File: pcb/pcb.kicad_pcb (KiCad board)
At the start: 2 copper layers, 58.9 x 71 mm, 19 parts, among them J1 CW308_WEST, J3 CW308_EAST, J4 CW308_SOUTH, J5 DEBUG, P1 WEST_PINS, P3 EAST_PINS, P4 SOUTH_PINS, SW1 RESET, U1 MSPM0L2228SPMR

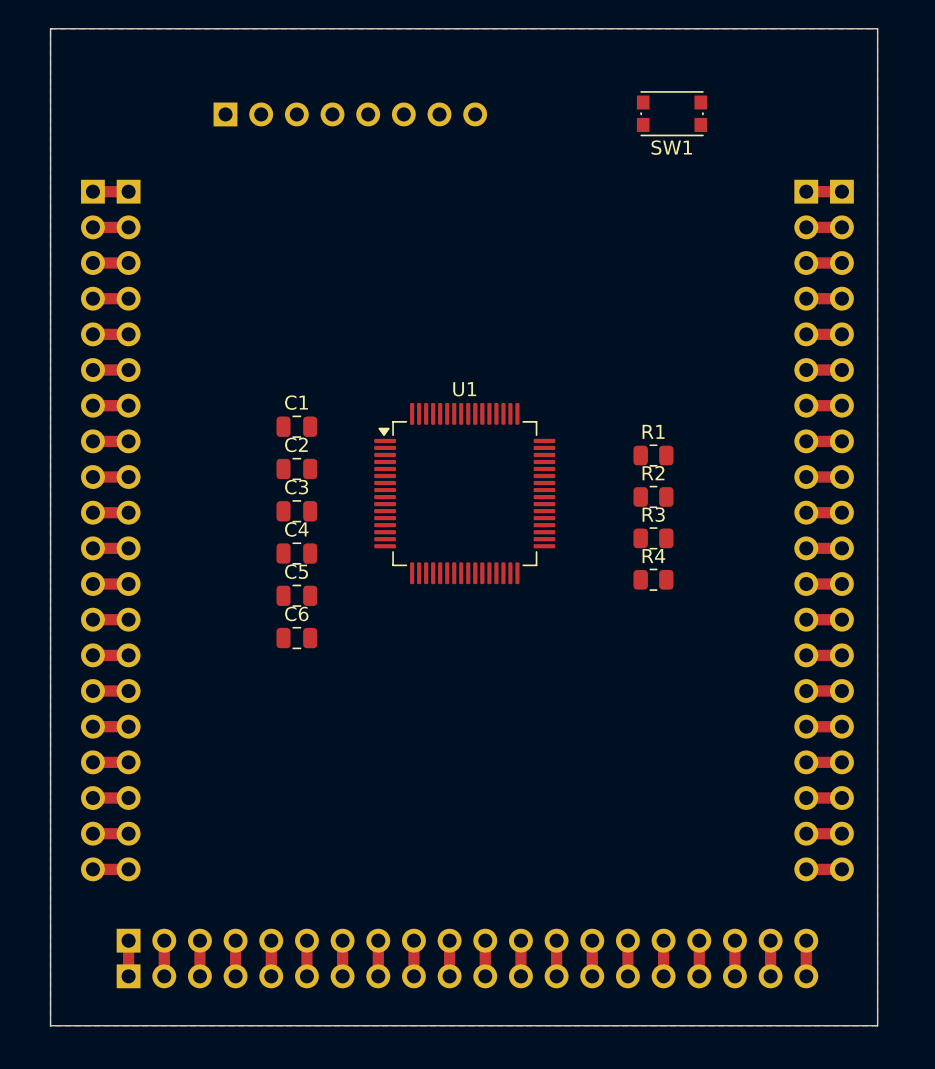
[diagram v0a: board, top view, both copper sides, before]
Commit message: PCB: auto-place and single-sided route, wire-jumper holes
Moved U1, the passives and SW1 (headers stay locked) and routed every
net on F.Cu only, with no vias. The 8 connections a single layer cannot
make get through-hole landing pads W1A..W8B (W2 lands on the J1-10 pin)
for wire jumpers on the back side.

Co-Authored-By: Claude Opus 5.5 <noreply@anthropic.com>
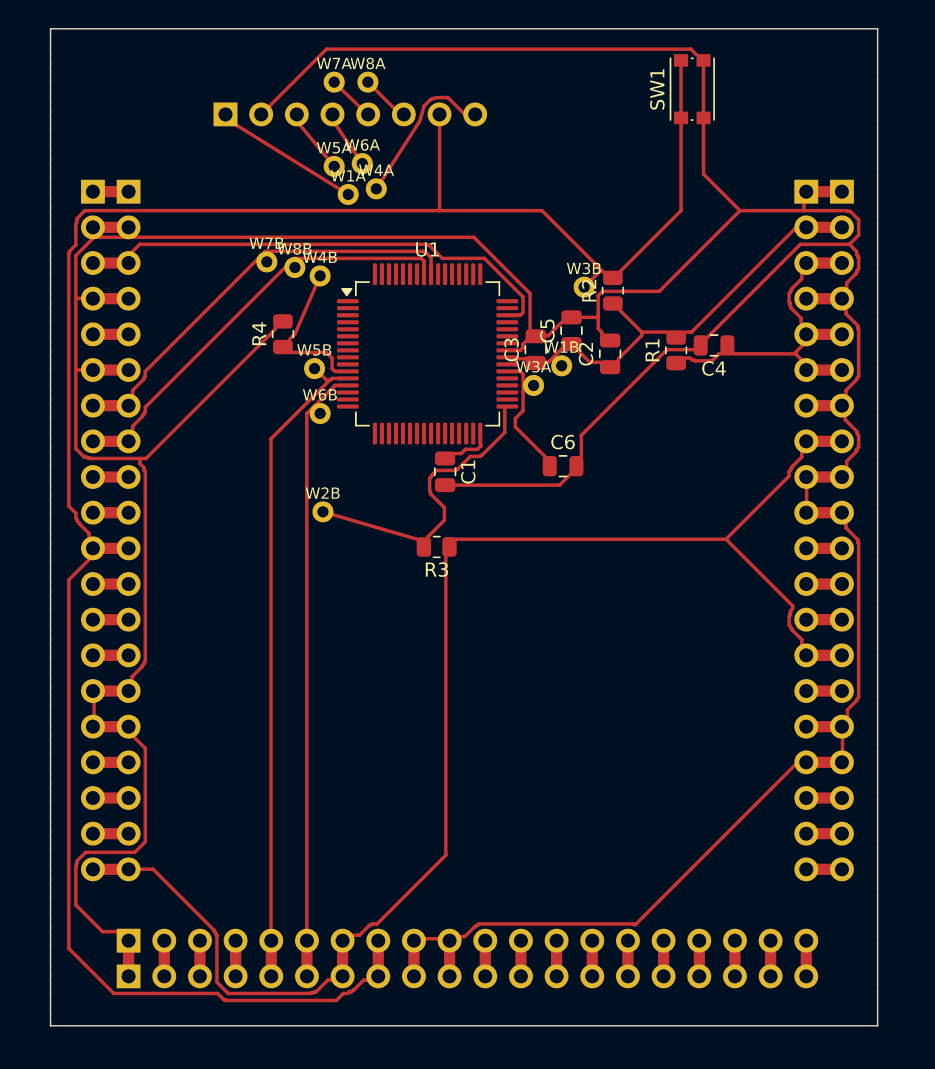
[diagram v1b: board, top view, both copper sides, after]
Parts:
- added W1A: Wire, , F.Cu at (69.7, 89.2)
- added W1B: Wire, , F.Cu at (84.9, 101.4)
- added W2B: Wire, , F.Cu at (67.9, 111.8)
- added W3A: Wire, , F.Cu at (82.9, 102.8)
- added W3B: Wire, , F.Cu at (86.5, 95.8)
- added W4A: Wire, , F.Cu at (71.7, 88.8)
- added W4B: Wire, , F.Cu at (67.7, 95.0)
- added W5A: Wire, , F.Cu at (68.7, 87.2)
- added W5B: Wire, , F.Cu at (67.3, 101.6)
- added W6A: Wire, , F.Cu at (70.7, 87.0)
- added W6B: Wire, , F.Cu at (67.7, 104.8)
- added W7A: Wire, , F.Cu at (68.7, 81.2)
- added W7B: Wire, , F.Cu at (63.9, 94.0)
- added W8A: Wire, , F.Cu at (71.1, 81.2)
- added W8B: Wire, , F.Cu at (65.9, 94.4)
- moved C4 33.2 mm to (95.8, 100.0), turned to 180 degrees
- moved R4 31.7 mm to (65.0, 99.2), turned to 90 degrees
- moved C5 27.2 mm to (85.6, 98.9), turned to 90 degrees
- moved C2 23.8 mm to (88.3, 100.5), turned to 90 degrees
- moved C6 22.6 mm to (85.0, 108.5)
- moved C3 20.5 mm to (83.0, 100.2), turned to 90 degrees
- moved R3 15.5 mm to (76.0, 114.3), turned to 180 degrees
- moved R2 15.0 mm to (88.5, 96.0), turned to 90 degrees
- moved C1 11.0 mm to (76.6, 109.0), turned to -90 degrees
- moved U1 10.3 mm to (75.3, 100.5)
- moved R1 7.66 mm to (93.0, 100.3), turned to 90 degrees
- moved SW1 2.27 mm to (94.2, 81.7), turned to 90 degrees
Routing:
- net Net-(J1-Pin_15): track 38.1 -> 314.2 mm
- net Net-(J1-Pin_11): track 5.08 -> 150.4 mm
- net Net-(J1-Pin_20): track 10.2 -> 97.7 mm
- net Net-(J4-Pin_5): track 2.54 -> 48.9 mm
- net Net-(J4-Pin_6): track 2.54 -> 45.5 mm
- net Net-(J3-Pin_2): track 2.54 -> 34.4 mm
- net Net-(J1-Pin_3): track 2.54 -> 33.8 mm
- net Net-(J1-Pin_8): track 2.54 -> 31.7 mm
- net Net-(J1-Pin_7): track 2.54 -> 31.6 mm
- net Net-(J1-Pin_10): track 2.54 -> 23.1 mm
- net Net-(J5-Pin_8): track 0.00 -> 19.6 mm
- net Net-(J3-Pin_3): track 7.62 -> 20.5 mm
- net Net-(U1-VCORE): track 0.00 -> 2.18 mm

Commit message: PCB: CNC-milled THT redesign, 1.0/0.5 mm, 8 wire jumpers, 3 mm fill isolation
Single-sided hat for the CW308-to-CW313 adapter, all copper on F.Cu, no vias.

- Through-hole parts: axial resistors, disc caps, 6 mm tactile switch.
- Milling rules (pcb.kicad_dru): 1.0 mm traces / 0.5 mm isolation; 0.3/0.2 mm only in the
  MSP fan-out area (MSP_FINE) and 0.35/0.2 mm between header pins (HDR_GAPS), 0.2 mm cutter.
  No-net copper fill keeps 3 mm from all copper, 1 mm minimum width, small islands removed.
- MSP pads lengthened to 0.3 x 2.5 mm for hand soldering.
- J5 reduced to 2 pins (BSL, GND); the debugger uses the P breakout headers.
- Trigger moved from PA0 to PB16 (MSP pin 4): firmware must follow.
- Outline widened to 62.5 x 72.05 mm (two traces fit outside the header rows).
- 8 wire jumpers with 12 dedicated holes; see pcb/wire-jumpers.md.
- CNC files (F.Cu, Edge.Cuts Gerbers with X2, Excellon drill) in pcb/cnc-files.

Co-Authored-By: Claude Opus 5.5 <noreply@anthropic.com>
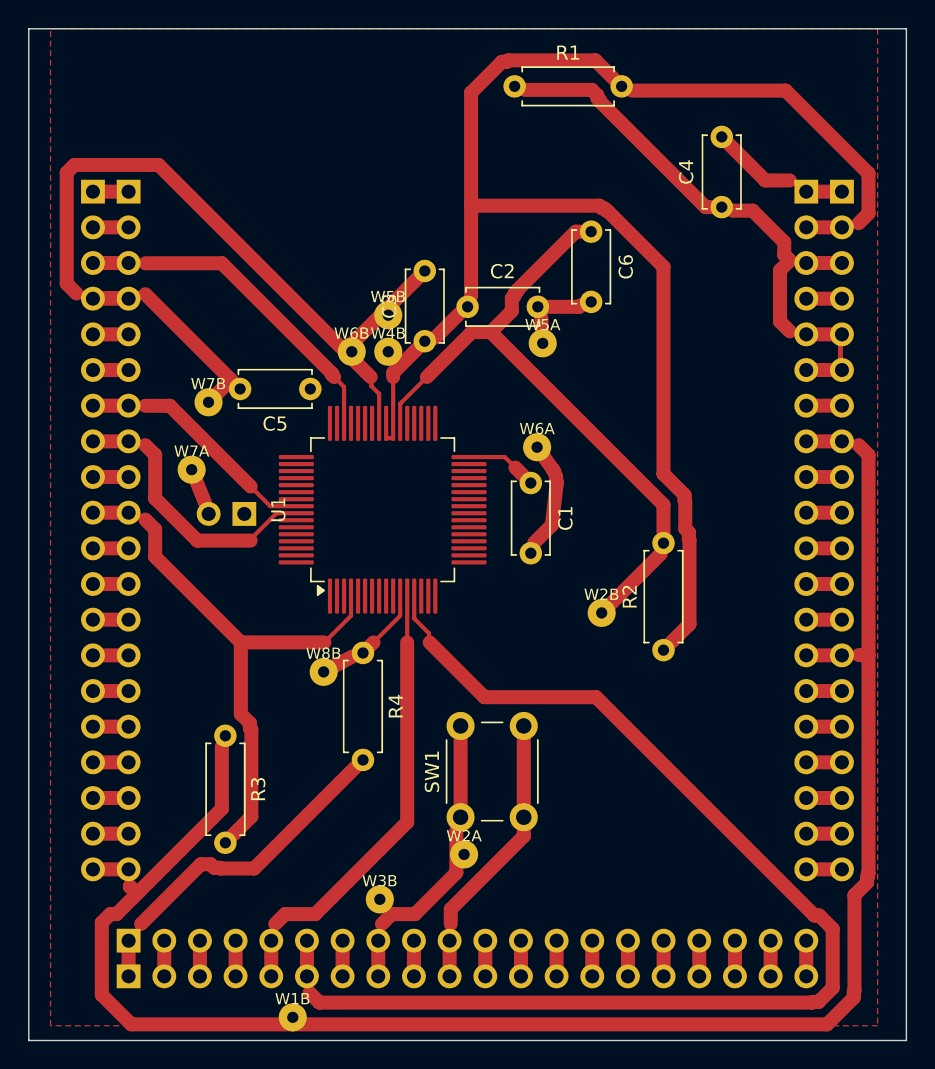
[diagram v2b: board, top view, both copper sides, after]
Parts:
- removed W1A, W3A, W4A, W8A: Wire, 
- added W2A: Wire, , F.Cu at (78.0, 136.2)
- C1, C2, C3, C4, C5, C6: footprint Capacitor_SMD:C_0805_2012Metric -> Capacitor_THT:C_Disc_D5.0mm_W2.5mm_P5.00mm
- J5: value DEBUG -> BSL_GND; footprint Connector_PinHeader_2.54mm:PinHeader_1x08_P2.54mm_Vertical -> Connector_PinHeader_2.54mm:PinHeader_1x02_P2.54mm_Vertical
- R1, R2, R3, R4: footprint Resistor_SMD:R_0805_2012Metric -> Resistor_THT:R_Axial_DIN0207_L6.3mm_D2.5mm_P7.62mm_Horizontal
- SW1: footprint Button_Switch_SMD:SW_Push_1P1T_NO_CK_KMR2 -> Button_Switch_THT:SW_PUSH_6mm
- moved SW1 54.4 mm to (77.7, 133.6)
- moved W1B 50.2 mm to (65.8, 147.8)
- moved W3B 46.0 mm to (72.0, 139.4)
- moved W7A 29.4 mm to (58.5, 108.8)
- moved W8B 28.9 mm to (68.0, 123.2)
- moved J5 28.5 mm to (62.3, 112.0), turned to 90 degrees
- moved R2 25.9 mm to (92.2, 121.7)
- moved W6A 23.7 mm to (83.2, 107.2)
- moved R4 23.4 mm to (70.8, 121.8), turned to -90 degrees
- moved R1 22.0 mm to (81.5, 81.5), turned to 0 degrees
- moved W2B 21.1 mm to (87.8, 119.0)
- moved R3 20.2 mm to (61.0, 127.8), turned to -90 degrees
- moved W5A 19.5 mm to (83.5, 99.8)
- moved C5 19.1 mm to (67.0, 103.0), turned to 180 degrees
- moved C6 16.8 mm to (87.0, 91.8), turned to -90 degrees
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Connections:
- J1 pad 10: Net-(J1-Pin_10) -> /TRIG
- J5 pad 1: Net-(J3-Pin_2) -> Net-(J5-Pin_1)
- P1 pad 10: Net-(J1-Pin_10) -> /TRIG
- R3 pad 2: Net-(J1-Pin_10) -> /TRIG
- R4 pad 1: Net-(J5-Pin_8) -> Net-(J5-Pin_1)
- U1 pad 11: Net-(J5-Pin_8) -> Net-(J5-Pin_1)
- U1 pad 33: Net-(J1-Pin_10) -> unconnected-(U1-PA0-Pad33)
- U1 pad 4: unconnected-(U1-PB16-Pad4) -> /TRIG
- W1B pad 1: Net-(J3-Pin_2) -> Net-(J1-Pin_20)
- W2B pad 1: Net-(J1-Pin_10) -> Net-(J1-Pin_11)
- W4B pad 1: Net-(J5-Pin_8) -> Net-(J3-Pin_2)
- W5A pad 1: Net-(J4-Pin_5) -> Net-(J1-Pin_15)
- W5B pad 1: Net-(J4-Pin_5) -> Net-(J1-Pin_15)
- W6A pad 1: Net-(J4-Pin_6) -> Net-(J1-Pin_15)
- W6B pad 1: Net-(J4-Pin_6) -> Net-(J1-Pin_15)
- W7A pad 1: Net-(J1-Pin_7) -> Net-(J1-Pin_15)
- W7B pad 1: Net-(J1-Pin_7) -> Net-(J1-Pin_15)
- W8B pad 1: Net-(J1-Pin_8) -> Net-(J5-Pin_1)
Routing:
- net Net-(J1-Pin_15): track 314.2 -> 154.6 mm
- net Net-(J1-Pin_11): track 150.4 -> 63.9 mm
- net Net-(J3-Pin_2): track 34.4 -> 103.2 mm
- net Net-(J4-Pin_6): track 45.5 -> 84.8 mm
- net /TRIG: track 0.00 -> 38.0 mm
- net Net-(J1-Pin_20): track 97.7 -> 129.5 mm
- net Net-(J1-Pin_10): track 23.1 -> 0.00 mm
- net Net-(J5-Pin_8): track 19.6 -> 0.00 mm
- net Net-(J4-Pin_5): track 48.9 -> 30.2 mm
- net Net-(J3-Pin_3): track 20.5 -> 37.8 mm
- net Net-(J1-Pin_7): track 31.6 -> 15.4 mm
- net Net-(J1-Pin_8): track 31.7 -> 18.0 mm
- net Net-(J1-Pin_3): track 33.8 -> 22.1 mm
- net Net-(J5-Pin_1): track 0.00 -> 5.50 mm
- net Net-(U1-VCORE): track 2.18 -> 3.14 mm
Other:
- board size 58.9 x 71 mm -> 62.5 x 72 mm
